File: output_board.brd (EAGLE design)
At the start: 100 x 54.2 mm, 27 parts, among them IC1 LTV-846PDIP16, IC2 LTV-846PDIP16, IC3 LTV-846PDIP16, IC4 LTV-846PDIP16

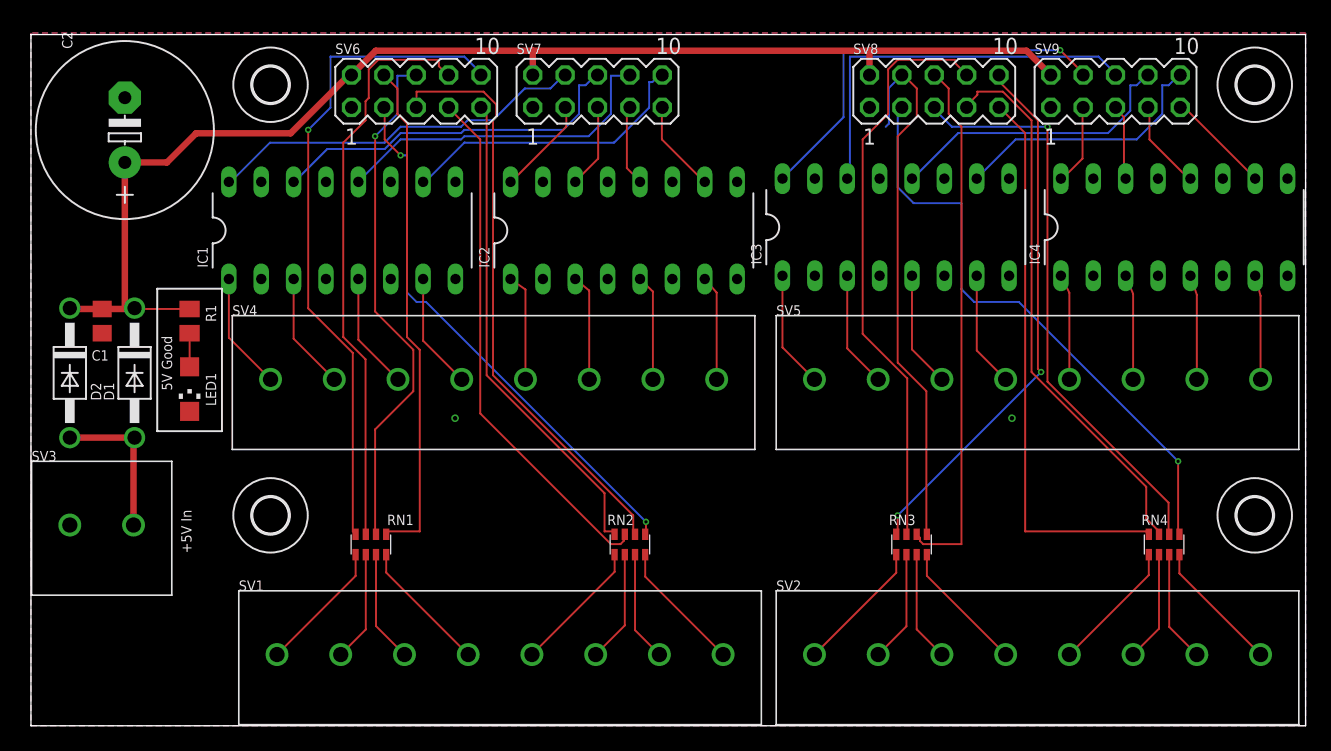
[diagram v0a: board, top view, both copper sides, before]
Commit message: Fixed bulk capacitor footprints; made +V for output channels independent on output board
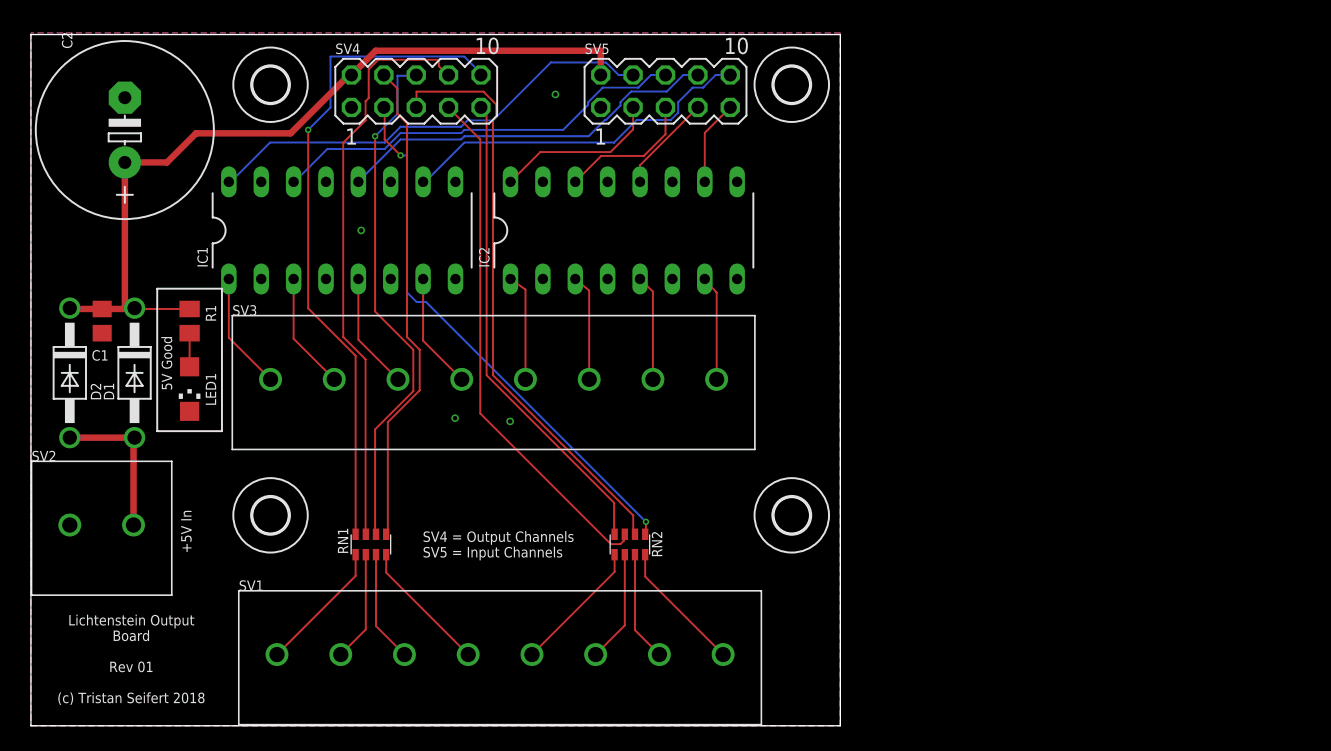
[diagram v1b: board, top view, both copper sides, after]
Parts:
- removed IC3, IC4: LTV-846PDIP16, lichtenstein_onion:DIL16
- removed RN3, RN4: 1k, resistor-net:CTS742C083
- removed SV6, SV7, SV8, SV9: (no value), con-lstb:MA05-2
- SV2: value 1792928 -> 1792863; device lichtenstein_onion:1792928 -> lichtenstein_onion:1792863
- SV3: value 1792863 -> 1792928; device lichtenstein_onion:1792863 -> lichtenstein_onion:1792928
- SV4, SV5: value 1792928 -> (none); device lichtenstein_onion:1792928 -> con-lstb:MA05-2
- moved SV2 59.3 mm to (3.05, 15.7)
- moved H1 36.3 mm to (59.7, 16.5)
- moved H3 36.3 mm to (59.7, 50.3)
- moved SV5 25.4 mm to (49.8, 49.8)
- moved SV4 25.3 mm to (30.2, 49.8)
- moved SV3 19.5 mm to (18.8, 27.2)
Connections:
- removed net IN10: IC3.5, SV5.3
- removed net IN11: IC3.7, SV5.4
- removed net IN12: IC4.1, SV5.5
- removed net IN13: IC4.3, SV5.6
- removed net IN14: IC4.5, SV5.7
- removed net IN15: IC4.7, SV5.8
- removed net IN8: IC3.1, SV5.1
- removed net IN9: IC3.3, SV5.2
- removed net INPUT10: IC3.12, SV9.8
- removed net INPUT11: IC3.10, SV9.10
- removed net INPUT12: IC4.16, SV9.3
- removed net INPUT13: IC4.14, SV9.5
- removed net INPUT14: IC4.12, SV9.7
- removed net INPUT15: IC4.10, SV9.9
- removed net INPUT8: IC3.16, SV9.4
- removed net INPUT9: IC3.14, SV9.6
- removed net OUT10: RN3.3, SV2.3
- removed net OUT11: RN3.4, SV2.4
- removed net OUT12: RN4.1, SV2.5
- removed net OUT13: RN4.2, SV2.6
- removed net OUT14: RN4.3, SV2.7
- removed net OUT15: RN4.4, SV2.8
- removed net OUT8: RN3.1, SV2.1
- removed net OUT9: RN3.2, SV2.2
- removed net OUTPUT10: RN3.6, SV8.6
- removed net OUTPUT11: RN3.5, SV8.4
- removed net OUTPUT12: RN4.8, SV8.9
- removed net OUTPUT13: RN4.7, SV8.7
- removed net OUTPUT14: RN4.6, SV8.5
- removed net OUTPUT15: RN4.5, SV8.3
- removed net OUTPUT8: RN3.8, SV8.10
- removed net OUTPUT9: RN3.7, SV8.8
- net +5V: now also SV4.2, SV5.2; no longer SV6.2, SV7.2, SV8.2, SV9.2
- net GND: now also SV2.1, SV4.1, SV5.1; no longer IC3.11, IC3.13, IC3.15, IC3.2, IC3.4, IC3.6, IC3.8, IC3.9, IC4.11, IC4.13, IC4.15, IC4.2, IC4.4, IC4.6, IC4.8, IC4.9, SV3.1, SV6.1, SV7.1, SV8.1, SV9.1
- net IN0: now also SV3.1; no longer SV4.1
- net IN1: now also SV3.2; no longer SV4.2
- net IN2: now also SV3.3; no longer SV4.3
- net IN3: now also SV3.4; no longer SV4.4
- net IN4: now also SV3.5; no longer SV4.5
- net IN5: now also SV3.6; no longer SV4.6
- net IN6: now also SV3.7; no longer SV4.7
- net IN7: now also SV3.8; no longer SV4.8
- net INPUT0: now also SV5.4; no longer SV7.4
- net INPUT1: now also SV5.6; no longer SV7.6
- net INPUT2: now also SV5.8; no longer SV7.8
- net INPUT3: now also SV5.10; no longer SV7.10
- net INPUT4: now also SV5.3; no longer SV7.3
- net INPUT5: now also SV5.5; no longer SV7.5
- net INPUT6: now also SV5.7; no longer SV7.7
- net INPUT7: now also SV5.9; no longer SV7.9
- net OUTPUT0: now also SV4.10; no longer SV6.10
- net OUTPUT1: now also SV4.8; no longer SV6.8
- net OUTPUT2: now also SV4.6; no longer SV6.6
- net OUTPUT3: now also SV4.4; no longer SV6.4
- net OUTPUT4: now also SV4.9; no longer SV6.9
- net OUTPUT5: now also SV4.7; no longer SV6.7
- net OUTPUT6: now also SV4.5; no longer SV6.5
- net OUTPUT7: now also SV4.3; no longer SV6.3
- net V+: now also SV2.2; no longer SV3.2
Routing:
- net OUTPUT15: track 47.2 -> 0.00 mm, vias 1 -> 0
- net OUTPUT9: track 45.9 -> 0.00 mm
- net OUTPUT14: track 45.7 -> 0.00 mm, vias 1 -> 0
- net OUTPUT12: track 43.9 -> 0.00 mm
- net OUTPUT13: track 43.4 -> 0.00 mm
- net OUTPUT11: track 42.7 -> 0.00 mm
- net OUTPUT8: track 42.1 -> 0.00 mm, vias 2 -> 0
- net OUTPUT10: track 41.7 -> 0.00 mm
- net +5V: track 102.6 -> 64.6 mm
- net INPUT8: track 31.7 -> 0.00 mm, vias 1 -> 0
- net INPUT9: track 31.2 -> 0.00 mm
- net INPUT10: track 23.0 -> 0.00 mm
- net INPUT11: track 20.6 -> 0.00 mm
- net OUT8: track 10.5 -> 0.00 mm
- net OUT15: track 10.5 -> 0.00 mm
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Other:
- board size 100 x 54.2 mm -> 63.5 x 54.2 mm
- board text added: "Lichtenstein Output Board Rev 01 (c) Tristan Seifert 2018"
- board text added: "SV4 = Output Channels SV5 = Input Channels"

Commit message: Cleaned up output board; added pull-ups to inputs on Lichtenstein board; moved some decoupling caps on FPGA output board
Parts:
- added R2, R3, R4, R5, R6, R7, R8, R9: 360R, rcl:M0805
- moved SV1 0.76 mm to (18.5, 5.59)
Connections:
- new net N$2: R2.1, SV3.8
- new net N$3: R3.1, SV3.7
- new net N$4: R4.1, SV3.6
- new net N$5: R5.1, SV3.5
- new net N$6: R6.1, SV3.4
- new net N$7: R7.1, SV3.3
- new net N$8: R8.1, SV3.2
- new net N$9: R9.1, SV3.1
- net IN0: now also R9.2; no longer SV3.1
- net IN1: now also R8.2; no longer SV3.2
- net IN2: now also R7.2; no longer SV3.3
- net IN3: now also R6.2; no longer SV3.4
- net IN4: now also R5.2; no longer SV3.5
- net IN5: now also R4.2; no longer SV3.6
- net IN6: now also R3.2; no longer SV3.7
- net IN7: now also R2.2; no longer SV3.8
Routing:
- net IN5: track 8.39 -> 3.78 mm
- net IN4: track 8.48 -> 3.88 mm
- net IN2: track 9.16 -> 4.62 mm
- net IN6: track 8.30 -> 3.78 mm
- net IN3: track 9.13 -> 4.62 mm
- net IN0: track 9.23 -> 4.72 mm
- net IN1: track 9.20 -> 4.72 mm
- net IN7: track 8.22 -> 4.03 mm
- net N$4: track 0.00 -> 2.65 mm
- net N$7: track 0.00 -> 2.64 mm
- net N$8: track 0.00 -> 2.64 mm
- net N$5: track 0.00 -> 2.63 mm
- net N$3: track 0.00 -> 2.62 mm
- net N$6: track 0.00 -> 2.61 mm
- net N$9: track 0.00 -> 2.61 mm
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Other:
- board text added: "Inputs (Active High)"
- board text added: "Outputs"

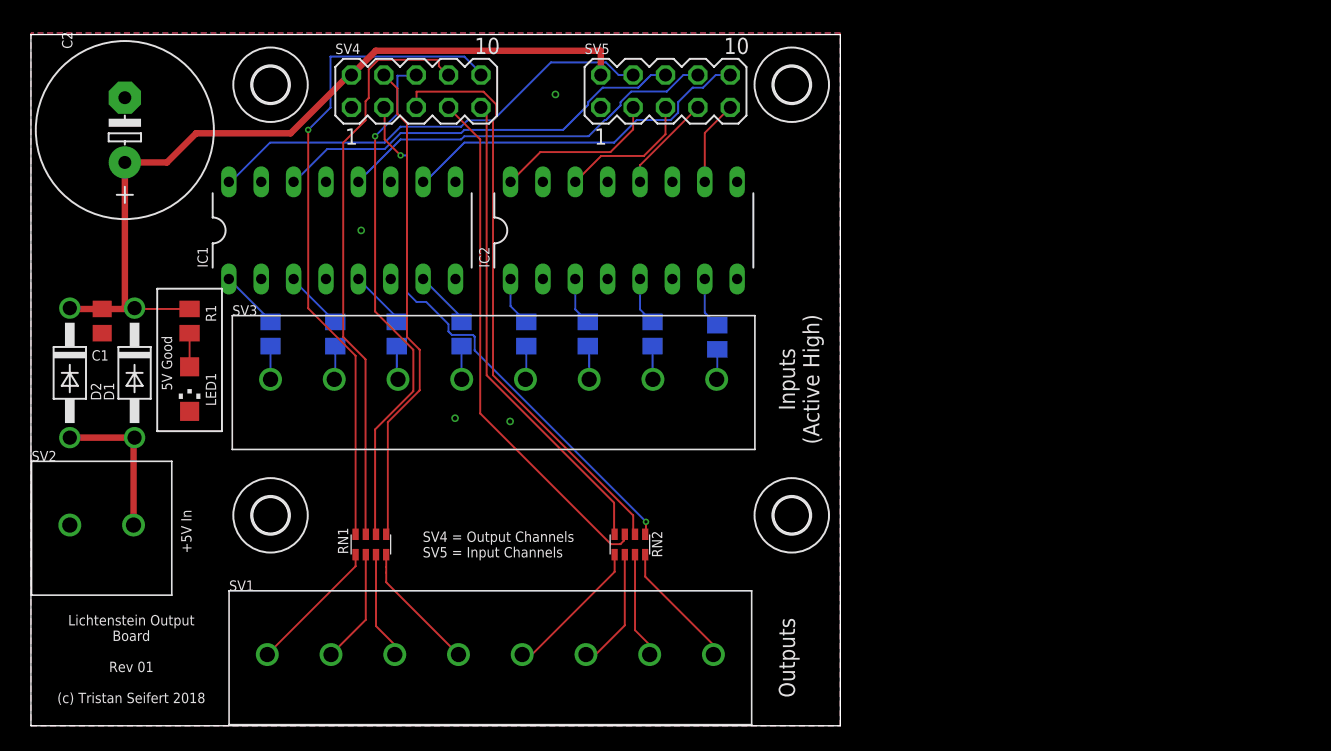
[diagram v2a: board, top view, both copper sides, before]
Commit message: Tweaked footprints for wire terminals; fixed up some mechanical issues on output board (incl. removing resistor networks)
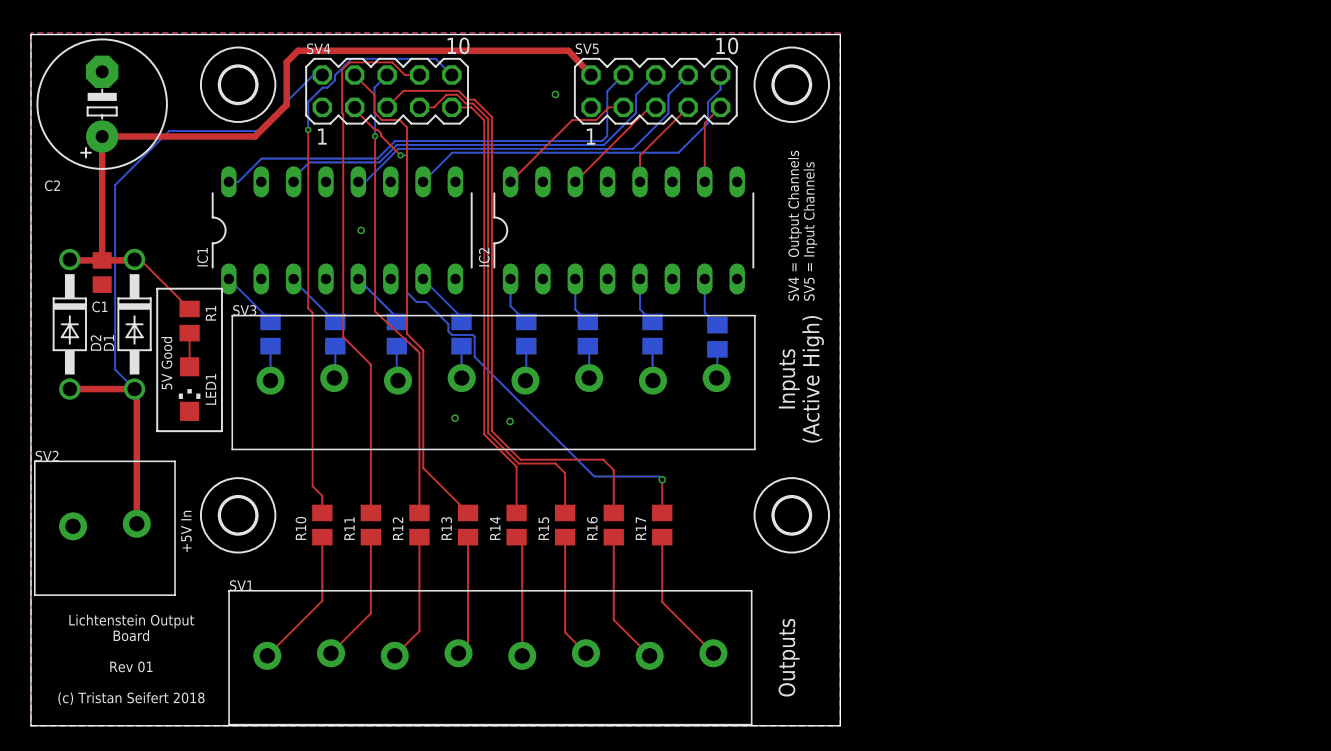
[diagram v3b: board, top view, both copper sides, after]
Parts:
- removed RN1, RN2: 1k, resistor-net:CTS742C083
- added R10, R11, R12, R13, R14, R15, R16, R17: 1k, rcl:M0805
- C2: device rcl:E5-13 -> rcl:E5-10,5
- moved C1 3.81 mm to (5.59, 35.6)
- moved D1 3.81 mm to (8.13, 31.5)
- moved D2 3.81 mm to (3.05, 31.5)
- moved C2 2.70 mm to (5.59, 48.8)
- moved H2 2.54 mm to (16.3, 50.3)
- moved H4 2.54 mm to (16.3, 16.5)
- moved SV4 2.29 mm to (27.9, 49.8)
- moved SV5 0.76 mm to (49.0, 49.8)
- moved SV2 0.25 mm to (3.30, 15.7)
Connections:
- net +5V: no longer SV4.2
- net OUT0: now also R10.1; no longer RN1.1
- net OUT1: now also R11.1; no longer RN1.2
- net OUT2: now also R12.1; no longer RN1.3
- net OUT3: now also R13.1; no longer RN1.4
- net OUT4: now also R14.1; no longer RN2.1
- net OUT5: now also R15.1; no longer RN2.2
- net OUT6: now also R16.1; no longer RN2.3
- net OUT7: now also R17.1; no longer RN2.4
- net OUTPUT0: now also R10.2; no longer RN1.8
- net OUTPUT1: now also R11.2; no longer RN1.7
- net OUTPUT2: now also R12.2; no longer RN1.6
- net OUTPUT3: now also R13.2; no longer RN1.5
- net OUTPUT4: now also R14.2; no longer RN2.8
- net OUTPUT5: now also R15.2; no longer RN2.7
- net OUTPUT6: now also R16.2; no longer RN2.6
- net OUTPUT7: now also R17.2; no longer RN2.5
- net V+: now also SV4.2
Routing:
- net V+: track 12.0 -> 52.3 mm
- net OUTPUT0: track 52.2 -> 46.1 mm
- net OUTPUT2: track 40.7 -> 36.5 mm
- net OUTPUT4: track 37.9 -> 34.8 mm
- net OUTPUT1: track 45.5 -> 42.4 mm
- net OUTPUT7: track 43.7 -> 46.6 mm
- net OUT6: track 8.31 -> 10.5 mm
- net OUTPUT6: track 46.3 -> 48.4 mm
- net INPUT5: track 10.8 -> 8.74 mm
- net INPUT4: track 13.2 -> 11.3 mm
- net OUT4: track 11.3 -> 9.49 mm
- net OUT2: track 8.45 -> 10.1 mm
- net OUT1: track 8.97 -> 10.4 mm
- net +5V: track 64.6 -> 65.6 mm
- net OUT3: track 10.2 -> 9.42 mm
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
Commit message: Minor revisions to output board
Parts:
- R1: value 1k -> 360R
- moved C1 6.86 mm to (5.59, 42.4), flipped to the bottom
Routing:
- net +5V: track 65.6 -> 68.3 mm, vias 0 -> 2
- net V+: track 52.3 -> 50.7 mm
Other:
- board text added: "(c) Tristan Seifert 2018"
- board text added: "Lichtenstein Output Board Rev 02"
- board text removed: "Lichtenstein Output Board Rev 01 (c) Tristan Seifert 2018"
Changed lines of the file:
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@@
 <text x="61.468" y="33.274" size="0.8128" layer="25" rot="R90">SV4 = Output Channels
 SV5 = Input Channels</text>
-<text x="7.874" y="1.778" size="0.8128" layer="25" align="bottom-center">Lichtenstein Output
-Board
-Rev 01
-(c) Tristan Seifert 2018</text>
+<text x="7.874" y="1.778" size="1.27" layer="25" align="bottom-center">Lichtenstein
+Output Board
+Rev 02</text>
 <text x="58.674" y="27.178" size="1.27" layer="25" rot="R90" align="top-center">Inputs
 (Active High)</text>
 <text x="58.674" y="5.334" size="1.27" layer="25" rot="R90" align="top-center">Outputs</text>
+<text x="40.132" y="2.794" size="0.8128" layer="26" rot="MR0" align="top-left">(c) Tristan Seifert 2018</text>
 </plain>
 <attributes>
@@
 <attribute name="SPICEPREFIX" value="C" x="5.588" y="48.768" size="1.778" layer="27" rot="R90" display="off"/>
 </element>
-<element name="C1" library="rcl" library_urn="urn:adsk.eagle:library:334" package="C0805" package3d_urn="urn:adsk.eagle:package:23617/2" value="100nF" x="5.588" y="35.56" smashed="yes" rot="R90">
-<attribute name="MOUSER" value="710-885012207072" x="5.588" y="35.56" size="1.778" layer="27" rot="R90" display="off"/>
-<attribute name="NAME" x="6.096" y="33.274" size="0.8128" layer="25" font="vector" ratio="10" rot="R180"/>
-<attribute name="SPICEPREFIX" value="C" x="5.588" y="35.56" size="1.778" layer="27" rot="R90" display="off"/>
+<element name="C1" library="rcl" library_urn="urn:adsk.eagle:library:334" package="C0805" package3d_urn="urn:adsk.eagle:package:23617/2" value="100nF" x="5.588" y="42.418" smashed="yes" rot="MR90">
+<attribute name="MOUSER" value="710-885012207072" x="5.588" y="42.418" size="1.778" layer="28" rot="MR90" display="off"/>
+<attribute name="NAME" x="5.08" y="40.132" size="0.8128" layer="26" font="vector" ratio="10" rot="MR180"/>
+<attribute name="SPICEPREFIX" value="C" x="5.588" y="42.418" size="1.778" layer="28" rot="MR90" display="off"/>
 </element>
 <element name="D1" library="diode" library_urn="urn:adsk.eagle:library:210" package="DO41-10" package3d_urn="urn:adsk.eagle:package:43336/1" value="1N4004" x="8.128" y="31.496" smashed="yes" rot="R270">
@@
 <attribute name="VALUE" x="9.906" y="27.686" size="1.27" layer="27" rot="R270"/>
 </element>
-<element name="R1" library="rcl" library_urn="urn:adsk.eagle:library:334" package="M0805" package3d_urn="urn:adsk.eagle:package:23556/1" value="1k" x="12.446" y="31.75" smashed="yes" rot="R270">
-<attribute name="MOUSER" value="652-CR0805JW-102ELF" x="12.446" y="31.75" size="1.778" layer="27" rot="R270" display="off"/>
+<element name="R1" library="rcl" library_urn="urn:adsk.eagle:library:334" package="M0805" package3d_urn="urn:adsk.eagle:package:23556/1" value="360R" x="12.446" y="31.75" smashed="yes" rot="R270">
+<attribute name="MOUSER" value="652-CR0805JW-361ELF" x="12.446" y="31.75" size="1.778" layer="27" rot="R270" display="off"/>
 <attribute name="NAME" x="13.716" y="33.02" size="0.8128" layer="25" font="vector" ratio="10" rot="R270"/>
 <attribute name="SPICEPREFIX" value="R" x="12.446" y="31.75" size="1.778" layer="27" rot="R270" display="off"/>
@@
 <contactref element="SV5" pad="2"/>
 <wire x1="3.048" y1="36.576" x2="3.048" y2="36.51" width="0.508" layer="1"/>
-<wire x1="3.048" y1="36.51" x2="5.588" y2="36.51" width="0.508" layer="1"/>
 <wire x1="8.128" y1="36.576" x2="8.128" y2="36.51" width="0.508" layer="1"/>
-<wire x1="8.128" y1="36.51" x2="5.588" y2="36.51" width="0.508" layer="1"/>
 <wire x1="7.366" y1="36.576" x2="8.128" y2="36.576" width="0.508" layer="1"/>
 <wire x1="42.164" y1="52.959" x2="43.942" y2="51.054" width="0.508" layer="1"/>
-<wire x1="5.588" y1="46.228" x2="5.588" y2="36.51" width="0.508" layer="1"/>
 <wire x1="12.446" y1="32.7" x2="8.57" y2="36.576" width="0.1524" layer="1"/>
 <wire x1="8.57" y1="36.576" x2="8.128" y2="36.576" width="0.1524" layer="1"/>
@@
 <wire x1="20.066" y1="48.71384375" x2="17.58015625" y2="46.228" width="0.508" layer="1"/>
 <wire x1="17.58015625" y1="46.228" x2="5.588" y2="46.228" width="0.508" layer="1"/>
+<via x="3.048" y="36.51" extent="1-16" drill="0.35"/>
+<via x="8.128" y="36.51" extent="1-16" drill="0.35"/>
+<wire x1="8.128" y1="36.576" x2="5.588" y2="36.576" width="0.508" layer="1"/>
+<wire x1="5.588" y1="36.576" x2="3.048" y2="36.576" width="0.508" layer="1"/>
+<wire x1="5.588" y1="46.228" x2="5.588" y2="36.576" width="0.508" layer="1"/>
+<wire x1="5.588" y1="43.368" x2="5.588" y2="46.228" width="0.508" layer="16"/>
 </signal>
 <signal name="V+">
@@
 <wire x1="8.128" y1="26.416" x2="3.048" y2="26.416" width="0.508" layer="1"/>
 <contactref element="SV4" pad="2"/>
-<wire x1="6.604" y1="27.94" x2="6.604" y2="42.418" width="0.1524" layer="16"/>
-<wire x1="6.604" y1="27.94" x2="8.128" y2="26.416" width="0.1524" layer="16"/>
 <wire x1="22.1547125" y1="51.054" x2="22.86" y2="51.054" width="0.1524" layer="16"/>
-<wire x1="10.8458" y1="46.6598" x2="17.7605125" y2="46.6598" width="0.1524" layer="16"/>
+<wire x1="13.462" y1="46.6598" x2="17.7605125" y2="46.6598" width="0.1524" layer="16"/>
 <wire x1="17.7605125" y1="46.6598" x2="22.1547125" y2="51.054" width="0.1524" layer="16"/>
-<wire x1="6.604" y1="42.418" x2="10.8458" y2="46.6598" width="0.1524" layer="16"/>
 <wire x1="8.302" y1="15.848" x2="8.302" y2="26.242" width="0.508" layer="1"/>
 <wire x1="8.302" y1="26.242" x2="8.128" y2="26.416" width="0.508" layer="1"/>
+<wire x1="8.128" y1="26.416" x2="6.604" y2="27.94" width="0.1524" layer="16"/>
+<wire x1="6.604" y1="39.8018" x2="13.462" y2="46.6598" width="0.1524" layer="16"/>
+<wire x1="6.604" y1="27.94" x2="6.604" y2="39.8018" width="0.1524" layer="16"/>
 </signal>
 <signal name="OUTPUT0">
